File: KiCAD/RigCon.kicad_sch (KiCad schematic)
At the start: 79 parts, among them J1 USB_C_Receptacle_USB2.0_16P, J2 PJ-320A, J3 PJ-320A, Q1 MMBT5551L, Q2 MMBT5551L, U1 UC EXPANSION, U10 USBLC6-2P6, U11 CH334P, U2 Speaker, U3 Speaker, U4 CP2102N-A02-GQFN24, U5 CM108B, U6 ADM3101E, U7 PCF8523T, U9 TPS2553, Y1 12MHz, Y3 32,768 kHz

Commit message: Updated PCB: routing added fox logo correct symbol for mounting hole with pad
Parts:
- added C30: 4.7uF, Capacitor_SMD:C_0402_1005Metric, symbol Device:C_Small
- added C31, C32: 47uF, Capacitor_SMD:C_0805_2012Metric, symbol Device:C_Small
- added L2: ~, uconsole:Logo_Fox, symbol uconsole:Logo
- added R7: 1k, Resistor_SMD:R_0402_1005Metric, symbol Device:R
- added TP7: 3V3, TestPoint:TestPoint_THTPad_D1.5mm_Drill0.7mm, symbol Connector:TestPoint
- BT1: footprint BK_940:MPD_BK-940 -> uconsole:MPD_BK-940; now fitted; now left out of the parts list
- C1, C18, C20, C21, C22, C3, C9: LCSC (none) -> C15525
- C10, C11, C12, C13, C14, C16, C17, C19, C2, C27, C4, C5, C8: LCSC (none) -> C1525
- C15, C29: LCSC (none) -> C52923
- C23, C24, C6, C7: LCSC (none) -> C1557
- C25, C26: LCSC (none) -> C32949
- C28: value 100uF -> 47uF; footprint Capacitor_SMD:C_0402_1005Metric -> Capacitor_SMD:C_0805_2012Metric; LCSC (none) -> C16780
- D1: LCSC (none) -> C91106
- H1, H2: footprint MountingHole:MountingHole_5mm -> MountingHole:MountingHole_5mm_Pad_Via; symbol Mechanical:MountingHole -> Mechanical:MountingHole_Pad; now fitted; now left out of the parts list
- J1, J2, J3, L1: now fitted; now left out of the parts list
- Q1, Q2: LCSC (none) -> C41095
- R1, R15, R16, R17: symbol Device:R_Small_US -> Device:R_Small; LCSC (none) -> C25752
- R11, R12, R18, R19, R2: symbol Device:R_Small_US -> Device:R_Small
- R20, R21: now left out of the parts list
- R22: value 100k -> 47k
- R4: value 100K -> 100k; symbol Device:R_Small_US -> Device:R_Small
- TH1: JLCPCB Part # C914089 -> (none); LCSC (none) -> C914089
- TP1, TP2, TP3, TP4, TP5, TP6: footprint footprints:TP -> TestPoint:TestPoint_THTPad_D1.5mm_Drill0.7mm
- U10: JLCPCB Part # C15999 -> (none); LCSC (none) -> C15999
- U11: LCSC (none) -> C5373042
- U4: LCSC (none) -> C969151
- U5: JLCPCB Part # C371347 -> (none); LCSC (none) -> C371347
- U6: LCSC (none) -> C514336
- U7: LCSC (none) -> C2651516
- U9: JLCPCB Part # C521201 -> (none); LCSC (none) -> C521201
- Y1: JLCPCB Part # C20617575 -> (none); LCSC (none) -> C20617575
- Y3: JLCPCB Part # C5119018 -> (none); LCSC (none) -> C5119018
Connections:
- net +3V3: now also TP7.1
- net +5V: now also R7.2; no longer U7.8 (VDD)
- net GND: now also C30.2, C31.2, C32.2
- net USB4_D+: now also U11.12 (DPU); no longer U11.11 (DMU)
- net USB4_D-: now also U11.11 (DMU); no longer U11.12 (DPU)
- net VBUS: now also C31.1, C32.1
- new net: C30.1, R7.1, U7.8 (VDD)
- no-connect marks 42 -> 44
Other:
- note added: "FOX"
- note added: "RigCon Extension Board"
- note removed: "Ham Extension Board"
- note removed: "Note:+3V3 was used on uConsole as well"
- title: uConsole expansion card template -> Rig Con Extension Board for ClockworkPi uConsole
- moved on the sheet: C27, R22, R3, R5, U9

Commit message: Fixed Errors in Labels excluded parts from position file and bom
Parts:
- JP1: footprint footprints:SolderJumper9-BCu -> uconsole:SolderJumper9-BCu
- JP2: footprint footprints:SolderJumper2-BCu -> uconsole:SolderJumper2-BCu
- JP3: footprint footprints:SolderJumper-BCu-Bridged -> uconsole:SolderJumper-BCu-Bridged
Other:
- title: Rig Con Extension Board for ClockworkPi uConsole -> RigCon Extension Board for ClockworkPi uConsole
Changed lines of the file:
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@@
 	(paper "A3")
 	(title_block
-		(title "Rig Con Extension Board for ClockworkPi uConsole")
-		(date "2024-07-10")
-		(rev "0.5")
+		(title "RigCon Extension Board for ClockworkPi uConsole")
+		(date "2025-02-26")
+		(rev "1.0")
 	)
 	(junction
@@
 			)
 		)
-		(property "Footprint" "footprints:SolderJumper-BCu-Bridged"
+		(property "Footprint" "uconsole:SolderJumper-BCu-Bridged"
 			(at 161.29 46.99 0)
 			(effects
@@
 			)
 		)
-		(property "Footprint" "footprints:SolderJumper9-BCu"
+		(property "Footprint" "uconsole:SolderJumper9-BCu"
 			(at 120.65 213.36 0)
 			(effects
@@
 			)
 		)
-		(property "Footprint" "footprints:SolderJumper9-BCu"
+		(property "Footprint" "uconsole:SolderJumper9-BCu"
 			(at 146.05 213.36 0)
 			(effects
@@
 			)
 		)
-		(property "Footprint" "footprints:SolderJumper2-BCu"
+		(property "Footprint" "uconsole:SolderJumper2-BCu"
 			(at 173.99 198.12 0)
 			(effects
@@
 			)
 		)
-		(property "Footprint" "footprints:SolderJumper9-BCu"
+		(property "Footprint" "uconsole:SolderJumper9-BCu"
 			(at 152.4 220.98 0)
 			(effects

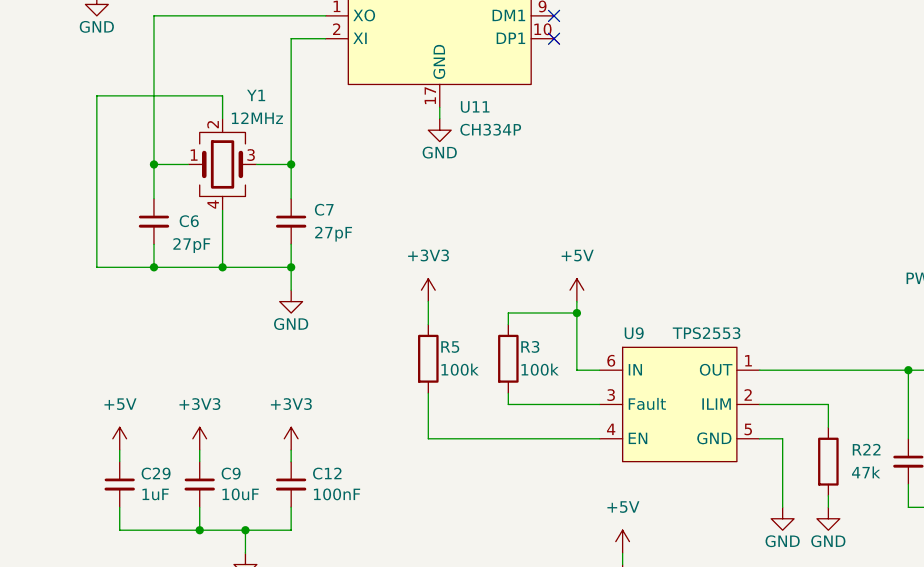
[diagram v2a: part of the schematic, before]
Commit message: Version of prototype order (v1.0)
Updated a few Texts and Order Numbers
Updated TPS2553 to TPS2553-1 (Latched version)
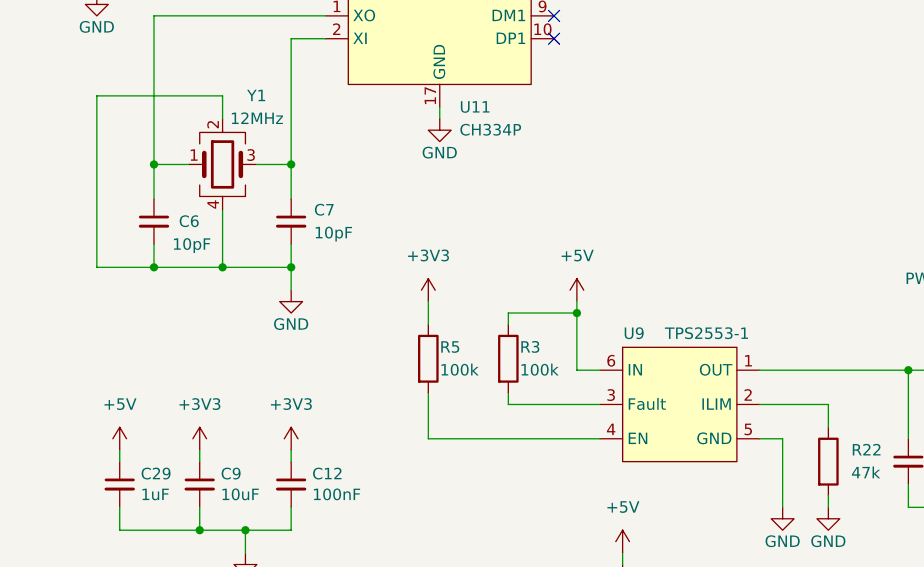
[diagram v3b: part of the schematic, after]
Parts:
- C6, C7: value 27pF -> 10pF
- L2, U1, U2, U3: now left out of the parts list
- U9: value TPS2553 -> TPS2553-1; LCSC C521201 -> C411878
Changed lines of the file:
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@@
 		(unit 1)
 		(exclude_from_sim no)
-		(in_bom yes)
+		(in_bom no)
 		(on_board yes)
 		(dnp no)
@@
 		(unit 1)
 		(exclude_from_sim no)
-		(in_bom yes)
+		(in_bom no)
 		(on_board yes)
 		(dnp no)
@@
 			)
 		)
-		(property "Value" "27pF"
+		(property "Value" "10pF"
 			(at 248.92 83.82 0)
 			(effects
@@
 		(unit 1)
 		(exclude_from_sim no)
-		(in_bom yes)
+		(in_bom no)
 		(on_board yes)
 		(dnp no)
@@
 			)
 		)
-		(property "Value" "27pF"
+		(property "Value" "10pF"
 			(at 237.49 85.09 0)
 			(effects
@@
 		(unit 1)
 		(exclude_from_sim no)
-		(in_bom yes)
+		(in_bom no)
 		(on_board yes)
 		(dnp no)
@@
 			)
 		)
-		(property "Value" "TPS2553"
+		(property "Value" "TPS2553-1"
 			(at 292.608 94.996 0)
 			(effects
@@
 			)
 		)
-		(property "LCSC" "C521201"
+		(property "LCSC" "C411878 "
 			(at 284.48 94.996 0)
 			(effects

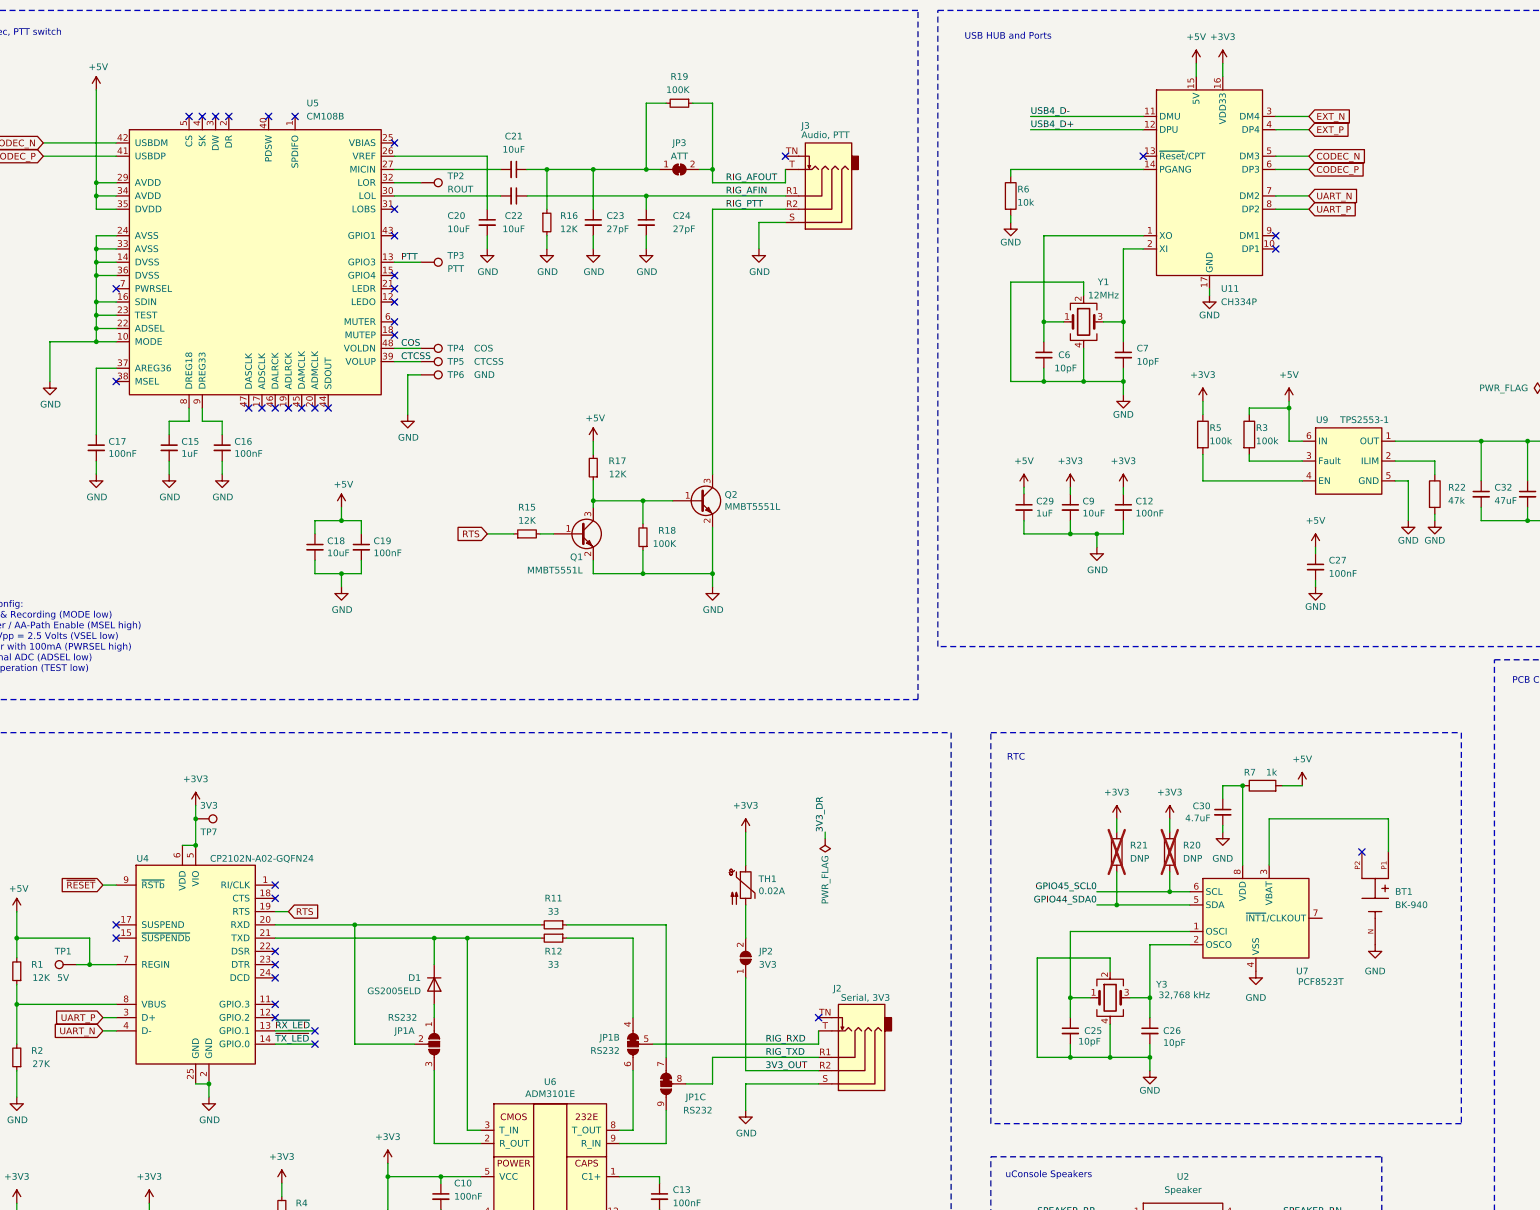
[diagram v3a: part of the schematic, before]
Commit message: Changes from RigCon version 1.0 to 1.1:
- changed clock crystal footprint
- removed I2C pullup resistor footprints (was DNP before)
- removed unneccessary load caps for clock crystal (RTC has internal ones)
- changed cap value on CM108B pin 37 to 10uF (NECESSARY!)
- removed GND connectrio on CM108B pin 16 SDIN (optional, simplified)

Added directory FrontPanel/ with dxf, openSCAD and stl files
Added Schematic to main dir
Added Render Pic of PCB to main dir
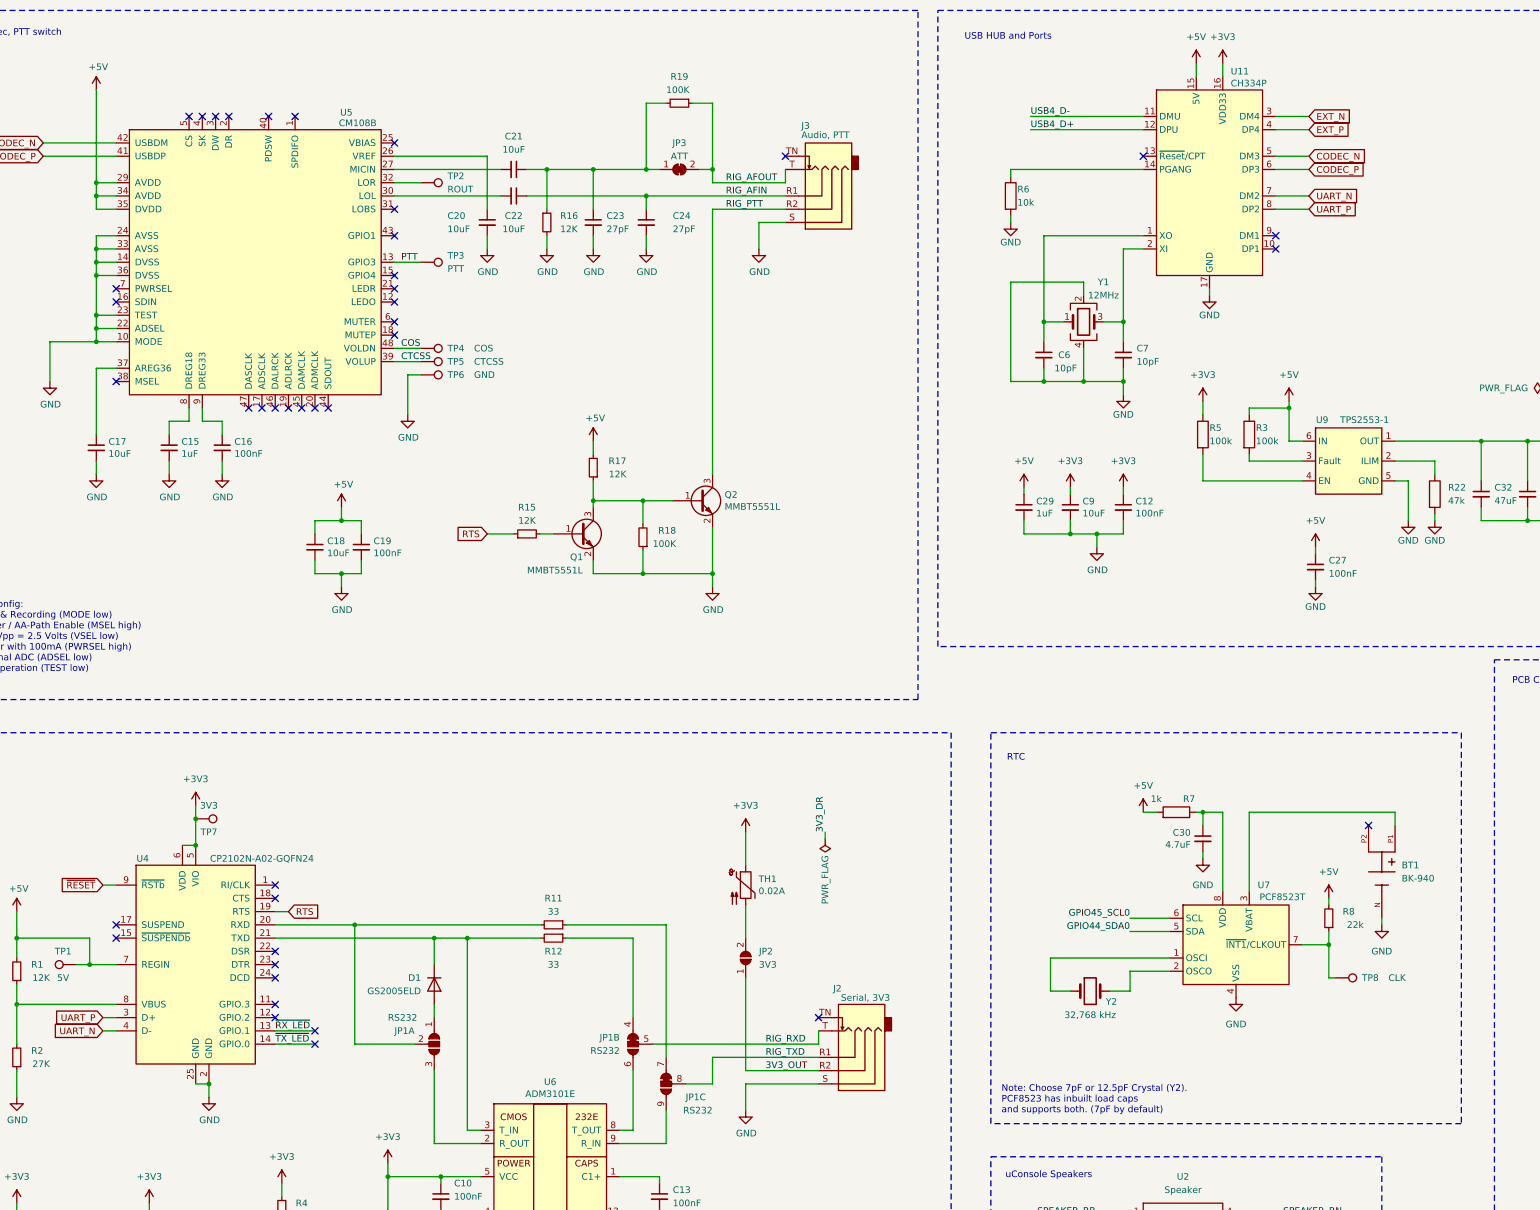
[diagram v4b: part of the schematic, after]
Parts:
- removed C25, C26: 10pF, Capacitor_SMD:C_0402_1005Metric, symbol Device:C_Small
- removed R20, R21: DNP, Resistor_SMD:R_0402_1005Metric, symbol Device:R
- added R8: 22k, Resistor_SMD:R_0402_1005Metric, symbol Device:R_Small
- added TP8: CLK, TestPoint:TestPoint_THTPad_D1.5mm_Drill0.7mm, symbol Connector:TestPoint
- C17: value 100nF -> 10uF
- Y2: renamed from Y3; footprint Crystal:Crystal_SMD_3225-4Pin_3.2x2.5mm -> Crystal:Crystal_SMD_3215-2Pin_3.2x1.5mm; symbol Device:Crystal_GND24 -> Device:Crystal
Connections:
- net +5V: now also R8.2
- net GND: no longer U5.16 (SDIN), Y2.2, Y2.4
- net at U7.2 (OSCO): now also Y2.2; no longer Y2.3
- net at U7.7 (~{INT1}/CLKOUT): now also R8.1, TP8.1
- no-connect marks 44 -> 45
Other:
- note added: "Note: Choose 7pF or 12.5pF Crystal (Y2). PCF8523 has inbuilt load caps and supports both. (7pF by default)"
- moved on the sheet: BT1, C30, R7, U7

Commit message: - Added Gerber, BOM & part positions for production - improved README
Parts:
- BT1: DigiKeyNr (none) -> BK-940
- C17: LCSC C1525 -> C15525
- J1: DigiKeyNr (none) -> USB4520-03-1-A
- J2, J3: DigiKeyNr (none) -> CP-SJ2-25774A-SMT
- Y2: LCSC C5119018 -> C97604
